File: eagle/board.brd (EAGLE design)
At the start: 11 parts, among them J1 M20X2SHROUDED

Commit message: Rename nets to match signal
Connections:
- net GPIO12 renamed DOOR_SWITCH
- net GPIO20 renamed LCK
- net GPIO21 renamed UNLCK
- net GPIO23 renamed SW_MOSI
- net GPIO24 renamed SW_MISO
- net GPIO25 renamed SW_SCLK
- removed net GPIO18: J1.12, RFID.3
- new net SSEL: J1.12
- new net SW_SSEL: RFID.3
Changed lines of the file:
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@@
 <wire x1="-16.51" y1="31.75" x2="-30.48" y2="-51.054" width="0" layer="19" extent="1-1"/>
 </signal>
-<signal name="GPIO18">
+<signal name="SSEL">
 <contactref element="J1" pad="12"/>
-<contactref element="RFID" pad="3"/>
-<wire x1="-16.51" y1="29.21" x2="-33.02" y2="-45.72" width="0" layer="19" extent="1-1"/>
 </signal>
-<signal name="GPIO23">
+<signal name="SW_MOSI">
 <contactref element="J1" pad="16"/>
 <contactref element="RFID" pad="4"/>
 <wire x1="-16.51" y1="24.13" x2="-30.48" y2="-45.974" width="0" layer="19" extent="1-1"/>
 </signal>
-<signal name="GPIO24">
+<signal name="SW_MISO">
 <contactref element="J1" pad="18"/>
 <contactref element="RFID" pad="5"/>
 <wire x1="-16.51" y1="21.59" x2="-27.94" y2="-45.72" width="0" layer="19" extent="1-1"/>
 </signal>
-<signal name="GPIO25">
+<signal name="SW_SCLK">
 <contactref element="J1" pad="22"/>
 <contactref element="RFID" pad="6"/>
@@
 <contactref element="J1" pad="28"/>
 </signal>
-<signal name="GPIO12">
+<signal name="DOOR_SWITCH">
 <contactref element="J1" pad="32"/>
 <contactref element="DOOR" pad="5"/>
@@
 <contactref element="J1" pad="36"/>
 </signal>
-<signal name="GPIO20">
+<signal name="LCK">
 <contactref element="J1" pad="38"/>
 <contactref element="DOOR" pad="2"/>
 <wire x1="-16.51" y1="-3.81" x2="-35.56" y2="-40.894" width="0" layer="19" extent="1-1"/>
 </signal>
-<signal name="GPIO21">
+<signal name="UNLCK">
 <contactref element="J1" pad="40"/>
 <contactref element="DOOR" pad="3"/>
@@
 <wire x1="-40.0812" y1="-11.1506" x2="-36.83" y2="-58.42" width="0" layer="19" extent="1-1"/>
 </signal>
+<signal name="SW_SSEL">
+<contactref element="RFID" pad="3"/>
+</signal>
 </signals>

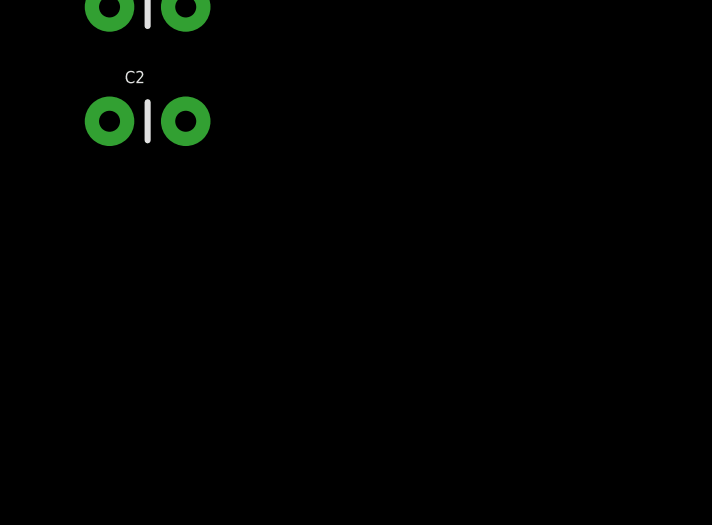
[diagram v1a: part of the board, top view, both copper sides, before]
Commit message: Connect LEDs
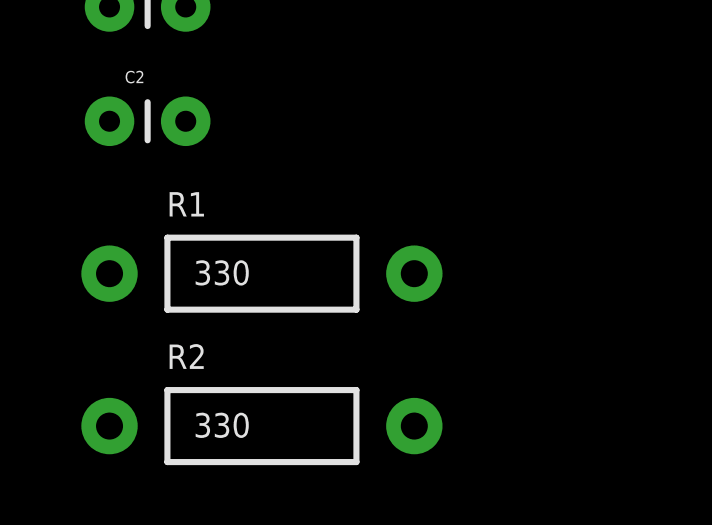
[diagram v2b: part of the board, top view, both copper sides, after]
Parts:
- added R1, R2: 330, SparkFun-Passives:AXIAL-0.4
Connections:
- removed net GPIO17: J1.11
- removed net GPIO27: J1.13
- removed net SSEL: J1.12
- new net LED0: D1.A, J1.11
- new net LED1: D2.A, J1.13
- new net N$2: D1.K, R1.P$1
- new net N$3: D2.K, R2.P$2
- net GND: now also R1.P$2, R2.P$1
- net SW_SSEL: now also J1.12
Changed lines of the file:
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@@
 <element name="C1" library="SparkFun-Passives" package="CAP-PTH-SMALL" value="10nF" x="-39.37" y="-54.61"/>
 <element name="C2" library="SparkFun-Passives" package="CAP-PTH-SMALL" value="10nF" x="-39.37" y="-58.42"/>
+<element name="R1" library="SparkFun-Passives" package="AXIAL-0.4" value="330" x="-34.29" y="-63.5"/>
+<element name="R2" library="SparkFun-Passives" package="AXIAL-0.4" value="330" x="-34.29" y="-68.58"/>
 </elements>
 <signals>
@@
 <wire x1="-16.51" y1="31.75" x2="-30.48" y2="-51.054" width="0" layer="19" extent="1-1"/>
 </signal>
-<signal name="SSEL">
-<contactref element="J1" pad="12"/>
-</signal>
 <signal name="SW_MOSI">
 <contactref element="J1" pad="16"/>
@@
 <contactref element="J1" pad="7"/>
 </signal>
-<signal name="GPIO17">
-<contactref element="J1" pad="11"/>
-</signal>
-<signal name="GPIO27">
-<contactref element="J1" pad="13"/>
-</signal>
 <signal name="GPIO22">
 <contactref element="J1" pad="15"/>
@@
 <contactref element="RFID" pad="2"/>
 <contactref element="GSM" pad="1"/>
+<contactref element="R1" pad="P$2"/>
+<contactref element="R2" pad="P$1"/>
+<wire x1="-29.21" y1="-63.5" x2="-39.37" y2="-68.58" width="0" layer="19" extent="1-1"/>
+<wire x1="-38.1" y1="-50.8" x2="-29.21" y2="-63.5" width="0" layer="19" extent="1-1"/>
 <wire x1="-35.56" y1="-45.974" x2="-38.1" y2="-50.8" width="0" layer="19" extent="1-1"/>
 <wire x1="-30.48" y1="-40.894" x2="-35.56" y2="-45.974" width="0" layer="19" extent="1-1"/>
@@
 <signal name="SW_SSEL">
 <contactref element="RFID" pad="3"/>
+<contactref element="J1" pad="12"/>
+<wire x1="-16.51" y1="29.21" x2="-33.02" y2="-45.72" width="0" layer="19" extent="1-1"/>
+</signal>
+<signal name="LED0">
+<contactref element="D1" pad="A"/>
+<contactref element="J1" pad="11"/>
+<wire x1="-19.05" y1="29.21" x2="-38.1" y2="-25.4" width="0" layer="19" extent="1-1"/>
+</signal>
+<signal name="LED1">
+<contactref element="D2" pad="A"/>
+<contactref element="J1" pad="13"/>
+<wire x1="-19.05" y1="26.67" x2="-38.1" y2="-33.02" width="0" layer="19" extent="1-1"/>
+</signal>
+<signal name="N$2">
+<contactref element="D1" pad="K"/>
+<contactref element="R1" pad="P$1"/>
+<wire x1="-35.56" y1="-25.4" x2="-39.37" y2="-63.5" width="0" layer="19" extent="1-1"/>
+</signal>
+<signal name="N$3">
+<contactref element="D2" pad="K"/>
+<contactref element="R2" pad="P$2"/>
+<wire x1="-35.56" y1="-33.02" x2="-29.21" y2="-68.58" width="0" layer="19" extent="1-1"/>
 </signal>
 </signals>
